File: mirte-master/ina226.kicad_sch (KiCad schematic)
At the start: 1 part, among them J7 INA226

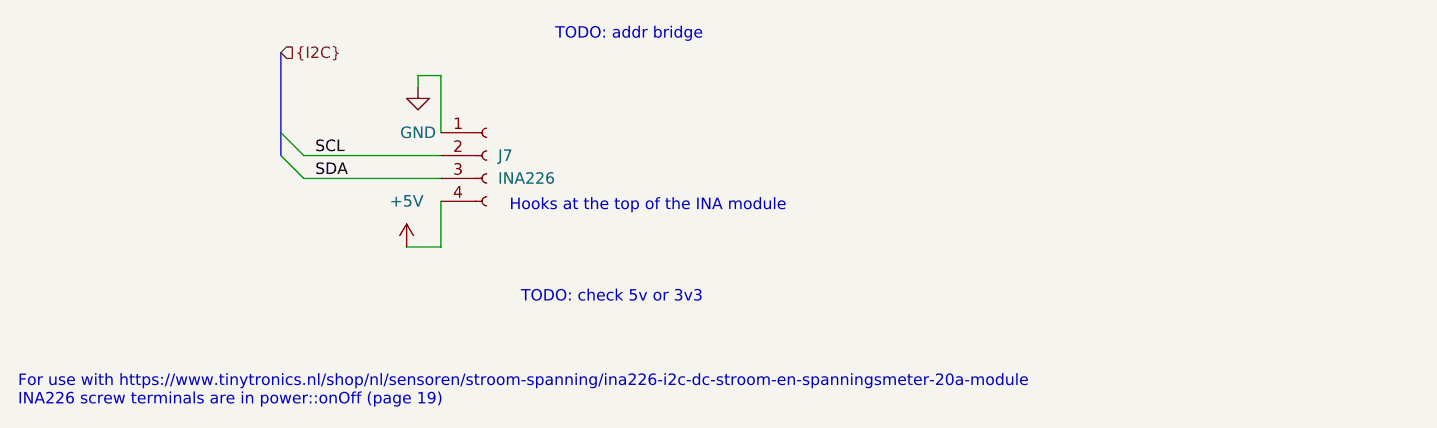
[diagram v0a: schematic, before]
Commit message: add kerco/elcos
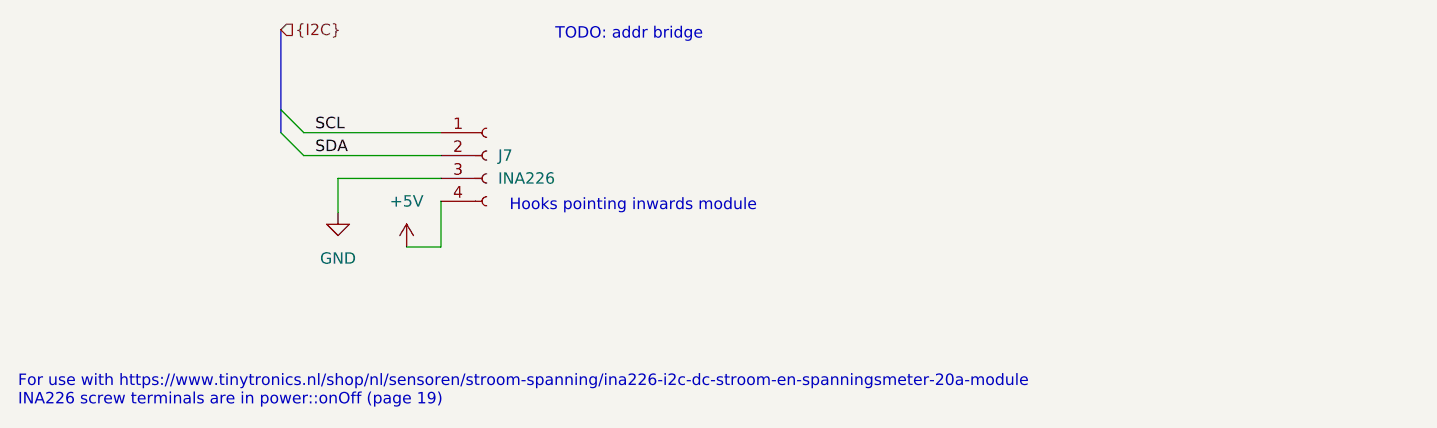
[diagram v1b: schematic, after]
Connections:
- net GND: now also J7.3 (Pin_3); no longer J7.1 (Pin_1)
- net SCL: now also J7.1 (Pin_1); no longer J7.2 (Pin_2)
- net SDA: now also J7.2 (Pin_2); no longer J7.3 (Pin_3)
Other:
- note added: "Hooks pointing inwards module"
- note removed: "Hooks at the top of the INA module"
- note removed: "TODO: check 5v or 3v3"
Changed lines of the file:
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@@
 (kicad_sch (version 20230121) (generator eeschema)
   (paper "A4")
+  (bus_entry (at 151.13 88.9) (size 2.54 2.54)
+    (stroke (width 0) (type default))
+  )
   (bus_entry (at 151.13 91.44) (size 2.54 2.54)
     (stroke (width 0) (type default))
   )
-  (bus_entry (at 151.13 93.98) (size 2.54 2.54)
+  (bus (pts (xy 151.13 80.01) (xy 151.13 88.9))
     (stroke (width 0) (type default))
   )
-  (bus (pts (xy 151.13 82.55) (xy 151.13 91.44))
+  (wire (pts (xy 157.48 100.33) (xy 157.48 96.52))
     (stroke (width 0) (type default))
   )
-  (wire (pts (xy 166.37 85.09) (xy 168.91 85.09))
+  (wire (pts (xy 153.67 91.44) (xy 168.91 91.44))
     (stroke (width 0) (type default))
   )
@@
     (stroke (width 0) (type default))
   )
-  (wire (pts (xy 168.91 85.09) (xy 168.91 91.44))
-    (stroke (width 0) (type default))
-  )
-  (wire (pts (xy 153.67 96.52) (xy 168.91 96.52))
-    (stroke (width 0) (type default))
-  )
   (wire (pts (xy 165.1 104.14) (xy 168.91 104.14))
     (stroke (width 0) (type default))
   )
-  (wire (pts (xy 166.37 85.09) (xy 166.37 86.36))
+  (wire (pts (xy 157.48 96.52) (xy 168.91 96.52))
     (stroke (width 0) (type default))
   )
-  (bus (pts (xy 151.13 91.44) (xy 151.13 93.98))
+  (bus (pts (xy 151.13 88.9) (xy 151.13 91.44))
     (stroke (width 0) (type default))
   )
@@
     (effects (font (size 1.27 1.27)) (justify left bottom))
   )
-  (text "TODO: check 5v or 3v3\n" (at 177.8 110.49 0)
-    (effects (font (size 1.27 1.27)) (justify left bottom))
-  )
-  (text "Hooks at the top of the INA module\n" (at 176.53 100.33 0)
+  (text "Hooks pointing inwards module\n" (at 176.53 100.33 0)
     (effects (font (size 1.27 1.27)) (justify left bottom))
   )
@@
     (effects (font (size 1.27 1.27)) (justify left bottom))
   )
-  (label "SDA" (at 154.94 96.52 0) (fields_autoplaced)
+  (label "SDA" (at 154.94 93.98 0) (fields_autoplaced)
     (effects (font (size 1.27 1.27)) (justify left bottom))
   )
-  (label "SCL" (at 154.94 93.98 0) (fields_autoplaced)
+  (label "SCL" (at 154.94 91.44 0) (fields_autoplaced)
     (effects (font (size 1.27 1.27)) (justify left bottom))
   )
-  (hierarchical_label "{I2C}" (shape input) (at 151.13 82.55 0) (fields_autoplaced)
+  (hierarchical_label "{I2C}" (shape input) (at 151.13 80.01 0) (fields_autoplaced)
     (effects (font (size 1.27 1.27)) (justify left))
   )
-  (symbol (lib_id "power:GND") (at 166.37 86.36 0) (unit 1)
+  (symbol (lib_id "power:GND") (at 157.48 100.33 0) (unit 1)
     (in_bom yes) (on_board yes) (dnp no) (fields_autoplaced)
-    (property "Reference" "#PWR018" (at 166.37 92.71 0)
+    (property "Reference" "#PWR018" (at 157.48 106.68 0)
       (effects (font (size 1.27 1.27)) hide)
     )
-    (property "Value" "GND" (at 166.37 91.44 0)
+    (property "Value" "GND" (at 157.48 105.41 0)
       (effects (font (size 1.27 1.27)))
     )
-    (property "Footprint" "" (at 166.37 86.36 0)
+    (property "Footprint" "" (at 157.48 100.33 0)
       (effects (font (size 1.27 1.27)) hide)
     )
-    (property "Datasheet" "" (at 166.37 86.36 0)
+    (property "Datasheet" "" (at 157.48 100.33 0)
       (effects (font (size 1.27 1.27)) hide)
     )
